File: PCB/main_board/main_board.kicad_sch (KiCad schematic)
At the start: 49 parts, among them CN1 XT30PW-M, CN2 XT30PW-M, U1 XT30PW-F, U3 W25N01GVZEIG_C907680, U4 INA226, U5 INA226, U6 RP2040, U7 AZ1117-3.3, X1 X322512MSB4SI

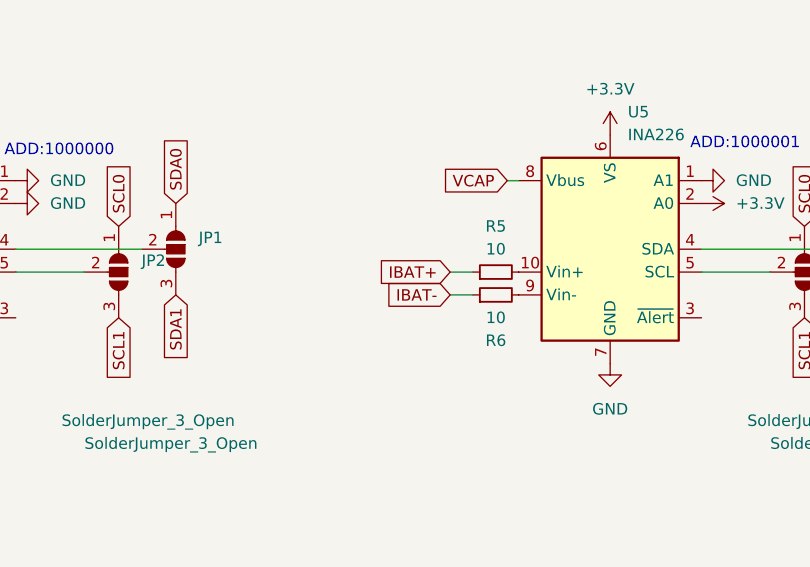
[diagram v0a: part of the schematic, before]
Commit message: Change INA226 connection
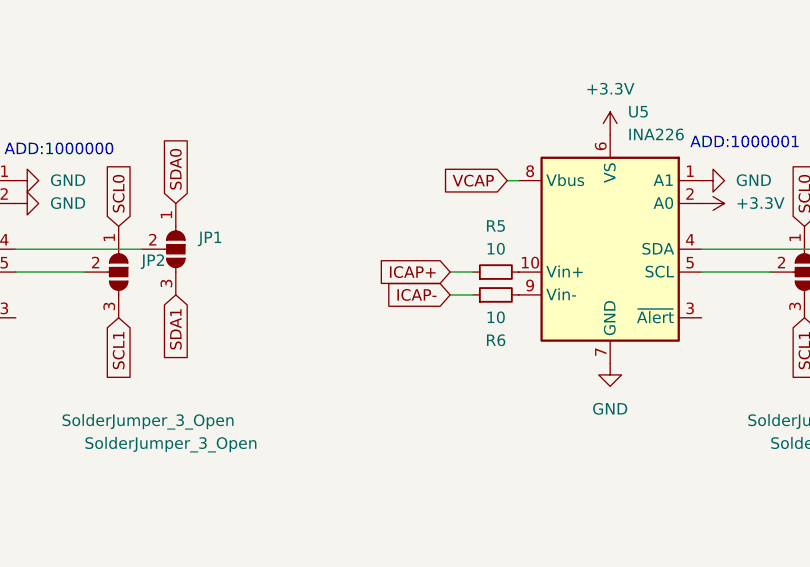
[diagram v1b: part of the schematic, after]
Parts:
- C1, C16, C17: footprint (none) -> Capacitor_SMD:C_0603_1608Metric
- JP5: footprint (none) -> Jumper:SolderJumper-2_P1.3mm_Open_Pad1.0x1.5mm
- R15, R16, R17, R18, R19, R7: footprint (none) -> Resistor_SMD:R_0603_1608Metric
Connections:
- net IBAT+: no longer R5.1
- net ICAP+: now also R5.1
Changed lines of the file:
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@@
     )
   )
-  (global_label "IBAT+" (shape input) (at 123.19 107.95 180) (fields_autoplaced)
+  (global_label "ICAP+" (shape input) (at 123.19 107.95 180) (fields_autoplaced)
     (effects (font (size 1.27 1.27)) (justify right))
-    (property "Intersheetrefs" "${INTERSHEET_REFS}" (at 114.7808 107.95 0)
+    (property "Intersheetrefs" "${INTERSHEET_REFS}" (at 114.4784 107.95 0)
       (effects (font (size 1.27 1.27)) (justify right) hide)
     )
@@
     )
   )
-  (global_label "IBAT-" (shape input) (at 123.19 110.49 180) (fields_autoplaced)
+  (global_label "ICAP-" (shape input) (at 123.19 110.49 180) (fields_autoplaced)
     (effects (font (size 1.27 1.27)) (justify right))
-    (property "Intersheetrefs" "${INTERSHEET_REFS}" (at 114.7808 110.49 0)
+    (property "Intersheetrefs" "${INTERSHEET_REFS}" (at 114.4784 110.49 0)
       (effects (font (size 1.27 1.27)) (justify right) hide)
     )
@@
       (effects (font (size 1.27 1.27)) (justify right))
     )
-    (property "Footprint" "" (at 69.85 231.14 0)
+    (property "Footprint" "Capacitor_SMD:C_0603_1608Metric" (at 69.85 231.14 0)
       (effects (font (size 1.27 1.27)) hide)
     )
@@
       (effects (font (size 1.27 1.27)))
     )
-    (property "Footprint" "" (at 85.09 181.61 0)
+    (property "Footprint" "Resistor_SMD:R_0603_1608Metric" (at 85.09 181.61 0)
       (effects (font (size 1.27 1.27)) hide)
     )
@@
       (effects (font (size 1.27 1.27)) (justify right))
     )
-    (property "Footprint" "" (at 74.93 231.14 0)
+    (property "Footprint" "Capacitor_SMD:C_0603_1608Metric" (at 74.93 231.14 0)
       (effects (font (size 1.27 1.27)) hide)
     )
@@
       (effects (font (size 1.27 1.27)))
     )
-    (property "Footprint" "" (at 85.09 179.07 0)
+    (property "Footprint" "Resistor_SMD:R_0603_1608Metric" (at 85.09 179.07 0)
       (effects (font (size 1.27 1.27)) hide)
     )
@@
       (effects (font (size 1.27 1.27)))
     )
-    (property "Footprint" "" (at 63.5 173.99 0)
+    (property "Footprint" "Resistor_SMD:R_0603_1608Metric" (at 63.5 173.99 0)
       (effects (font (size 1.27 1.27)) hide)
     )
@@
       (effects (font (size 1.27 1.27)))
     )
-    (property "Footprint" "" (at 274.32 226.06 0)
+    (property "Footprint" "Jumper:SolderJumper-2_P1.3mm_Open_Pad1.0x1.5mm" (at 274.32 226.06 0)
       (effects (font (size 1.27 1.27)) hide)
     )
@@
       (effects (font (size 1.27 1.27)))
     )
-    (property "Footprint" "" (at 63.5 189.23 0)
+    (property "Footprint" "Resistor_SMD:R_0603_1608Metric" (at 63.5 189.23 0)
       (effects (font (size 1.27 1.27)) hide)
     )
@@
       (effects (font (size 1.27 1.27)))
     )
-    (property "Footprint" "" (at 265.43 193.04 0)
+    (property "Footprint" "Resistor_SMD:R_0603_1608Metric" (at 265.43 193.04 0)
       (effects (font (size 1.27 1.27)) hide)
     )
@@
       (effects (font (size 1.27 1.27)))
     )
-    (property "Footprint" "" (at 80.01 227.33 0)
+    (property "Footprint" "Resistor_SMD:R_0603_1608Metric" (at 80.01 227.33 0)
       (effects (font (size 1.27 1.27)) hide)
     )
@@
       (effects (font (size 1.27 1.27)) (justify left))
     )
-    (property "Footprint" "" (at 224.79 201.93 0)
-      (effects (font (size 1.27 1.27)) hide)
-    )
+    (property "Footprint" "Capacitor_SMD:C_0603_1608Metric" (at 224.79 201.93 0)
+      (effects (font (size 1.27 1.27)) hide)
+    )

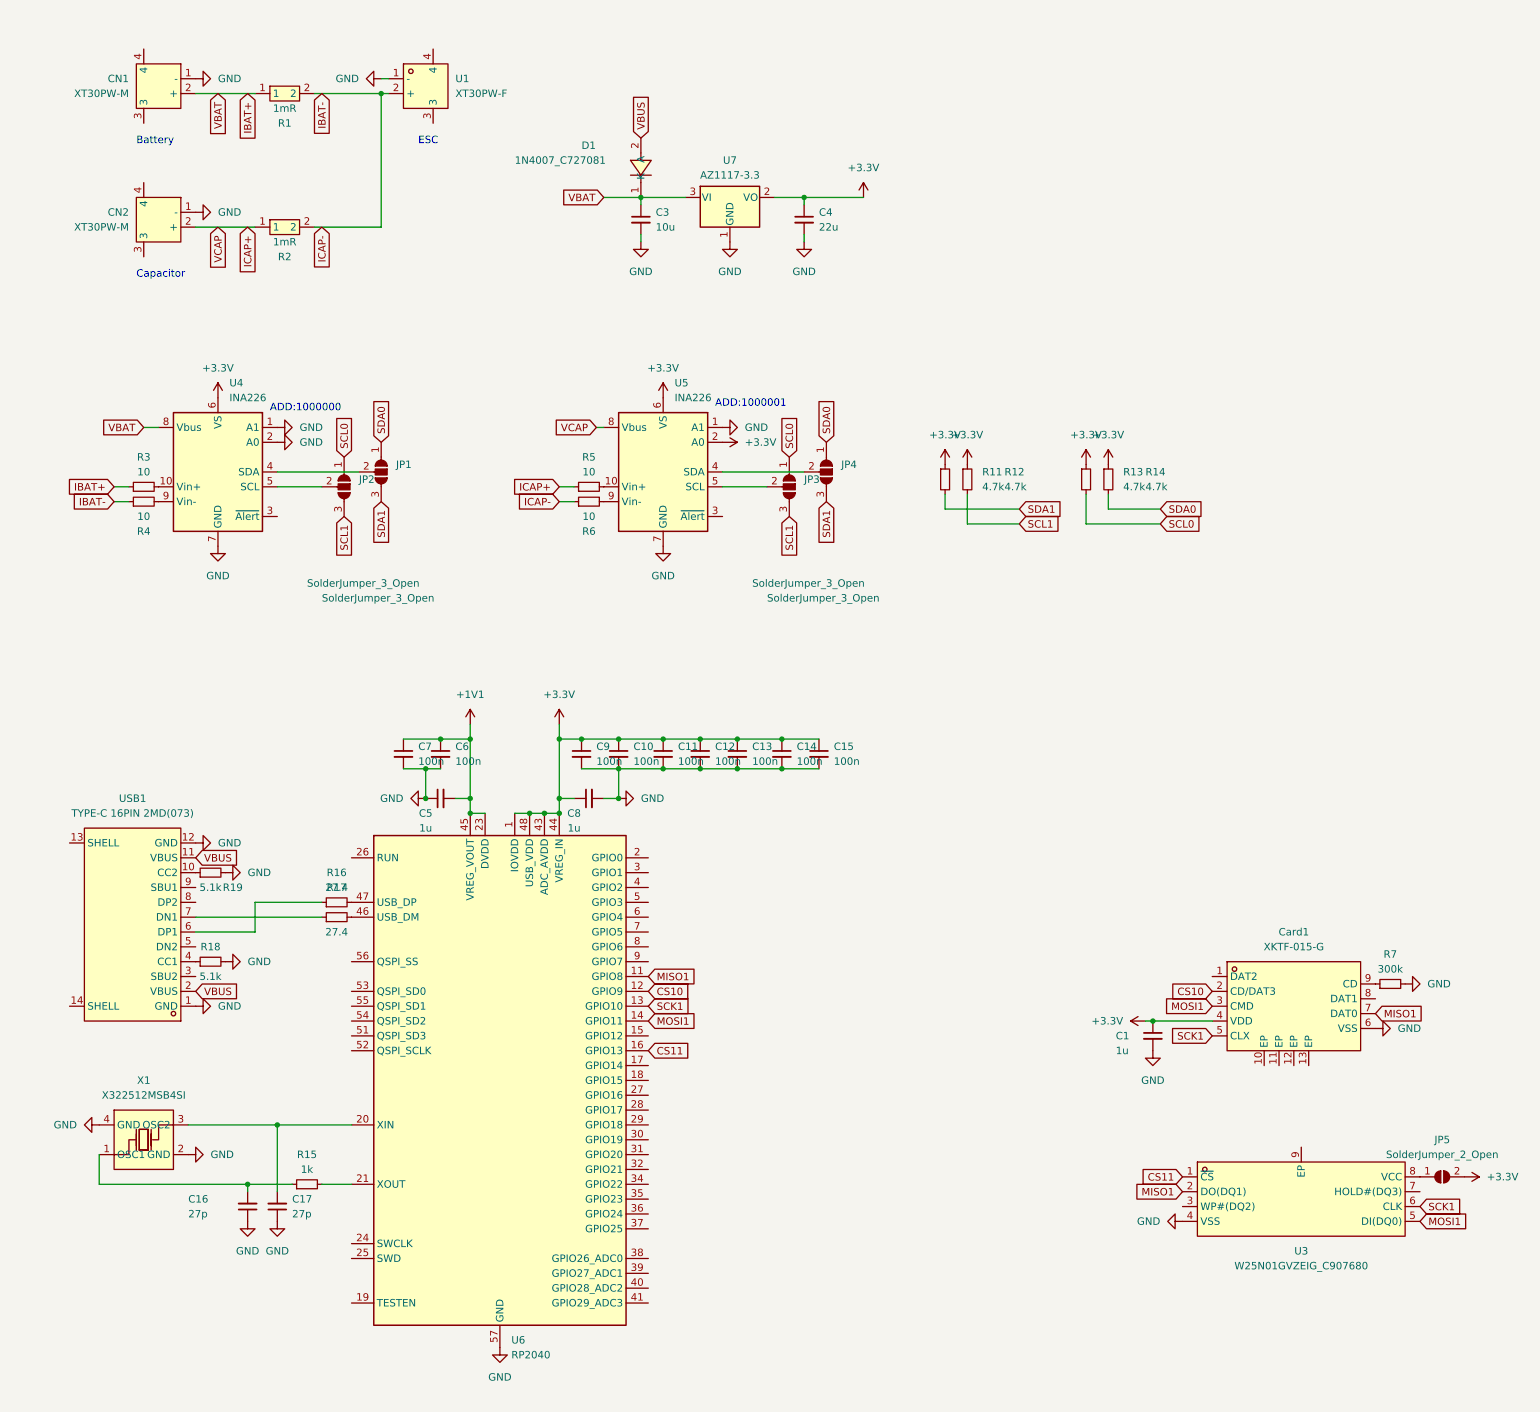
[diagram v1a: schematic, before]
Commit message: Add EEPROM to mcu; Change R and C to 0402
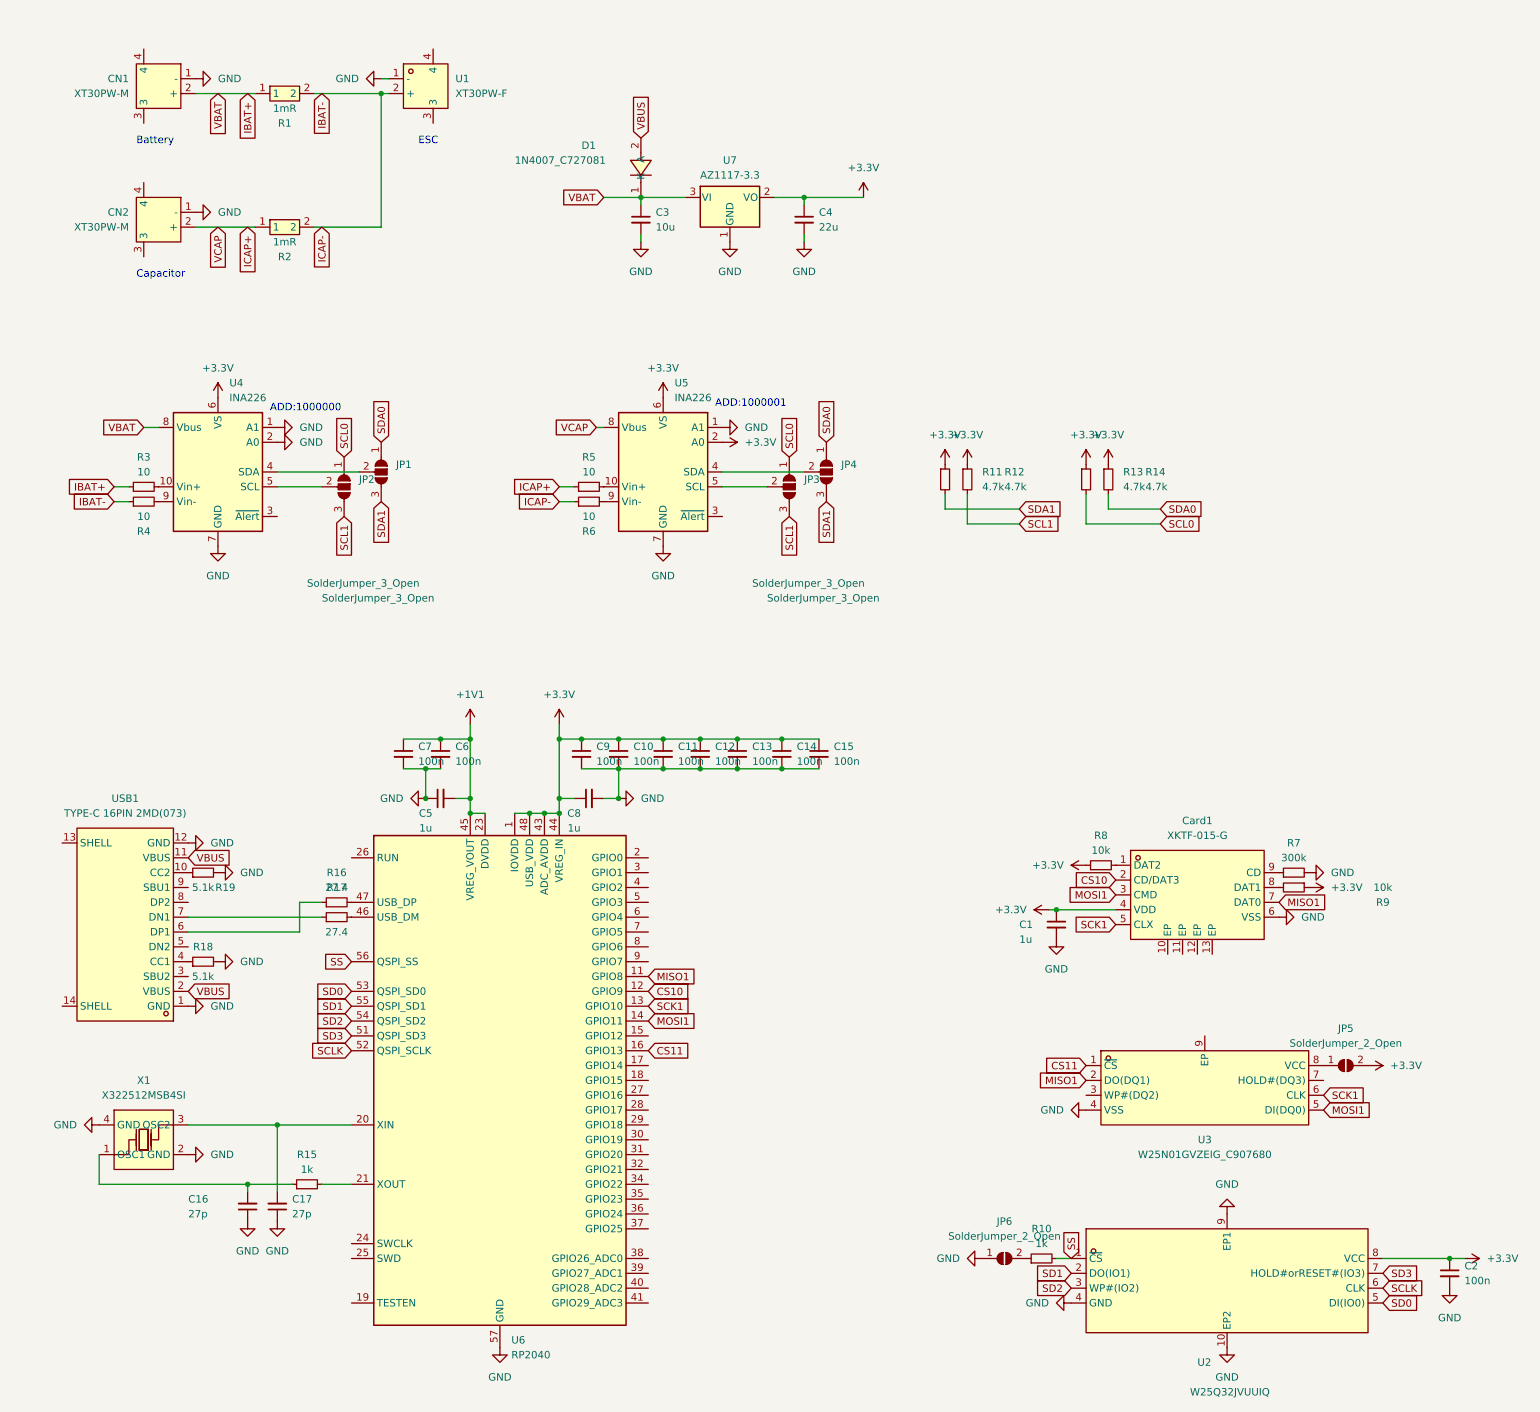
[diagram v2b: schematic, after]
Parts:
- added C2: 100n, Capacitor_SMD:C_0402_1005Metric, symbol Device:C_Small
- added JP6: SolderJumper_2_Open, Jumper:SolderJumper-2_P1.3mm_Open_Pad1.0x1.5mm, symbol Jumper:SolderJumper_2_Open
- added R10: 1k, Resistor_SMD:R_0402_1005Metric, symbol Device:R_Small
- added R8, R9: 10k, Resistor_SMD:R_0402_1005Metric, symbol Device:R_Small
- added U2: W25Q32JVUUIQ, pcb_lib:USON-8_L4.0-W3.0-P0.80-BL_WINBOND_UU, symbol pcb_lib:W25Q32JVUUIQ
- C1, C10, C11, C12, C13, C14, C15, C16, C17, C3, C4, C5, C6, C7, C8, C9: footprint Capacitor_SMD:C_0603_1608Metric -> Capacitor_SMD:C_0402_1005Metric
- CN1, CN2: footprint easyeda2kicad:CONN-TH_XT30PW-M -> pcb_lib:CONN-TH_XT30PW-M
- Card1: footprint easyeda2kicad:TF-SMD_XKTF-015-N -> pcb_lib:TF-SMD_XKTF-015-N
- D1: footprint easyeda2kicad:SMA_L4.3-W2.5-LS5.0-RD -> pcb_lib:SMA_L4.3-W2.5-LS5.0-RD
- R1, R2: footprint easyeda2kicad:R3920 -> pcb_lib:R3920
- R11, R12, R13, R14, R15, R16, R17, R18, R19, R3, R4, R5, R6, R7: footprint Resistor_SMD:R_0603_1608Metric -> Resistor_SMD:R_0402_1005Metric
- U1: footprint easyeda2kicad:CONN-TH_XT30PW-F-1 -> pcb_lib:CONN-TH_XT30PW-F-1
- U3: footprint easyeda2kicad:WSON-8_L8.0-W6.10-P1.27-BL-EP -> pcb_lib:WSON-8_L8.0-W6.10-P1.27-BL-EP
- USB1: footprint easyeda2kicad:USB-C-SMD_TYPE-C-6PIN-2MD-073 -> pcb_lib:USB-C-SMD_TYPE-C-6PIN-2MD-073
- X1: footprint easyeda2kicad:OSC-SMD_4P-L3.2-W2.5-BL -> pcb_lib:OSC-SMD_4P-L3.2-W2.5-BL
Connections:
- net +3.3V: now also C2.1, R8.1, R9.1, U2.8 (VCC)
- net GND: now also C2.2, JP6.1 (A), U2.10 (EP2), U2.4 (GND), U2.9 (EP1)
- net SD3: now reaches U6.51 (QSPI_SD3)
- net SD3: now also U2.7 (HOLD#orRESET#(IO3))
- net SCLK: now reaches U6.52 (QSPI_SCLK)
- net SCLK: now also U2.6 (CLK)
- net SD0: now reaches U6.53 (QSPI_SD0)
- net SD0: now also U2.5 (DI(IO0))
- net SD2: now reaches U6.54 (QSPI_SD2)
- net SD2: now also U2.3 (WP#(IO2))
- net SD1: now reaches U6.55 (QSPI_SD1)
- net SD1: now also U2.2 (DO(IO1))
- net SS: now reaches U6.56 (QSPI_SS)
- net SS: now also R10.2, U2.1 (~{CS})
- net at Card1.1 (DAT2): now also R8.2
- net at Card1.8 (DAT1): now also R9.2
- new net: JP6.2 (B), R10.1
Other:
- moved on the sheet: C1, Card1, JP5, R18, R19, R7, U3, USB1
